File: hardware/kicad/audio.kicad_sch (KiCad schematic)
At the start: 0 parts

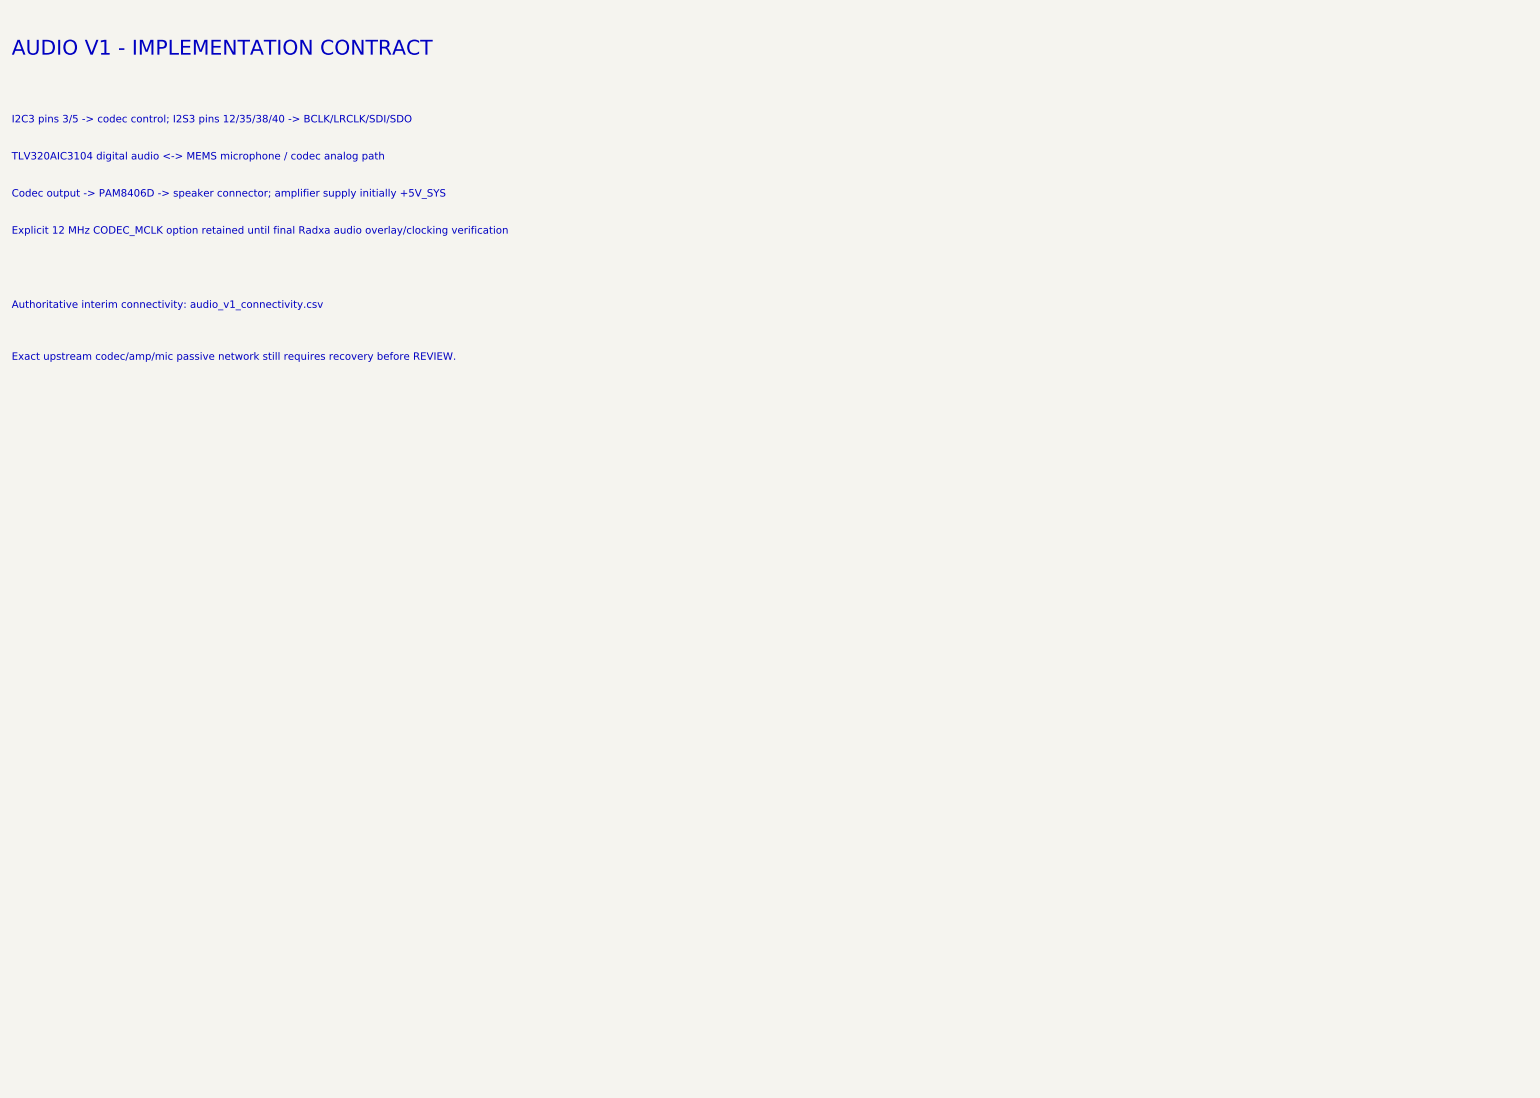
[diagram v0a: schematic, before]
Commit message: [verified] refactor(hardware): restore strict single-board Radxa port
Import the routed upstream Pollen Robot HAT as the active design, adapt the critical host nets for Radxa ZERO 3W, remove the divergent high-current redesign artifacts, and add regenerated baseline-aware KiCad validation.
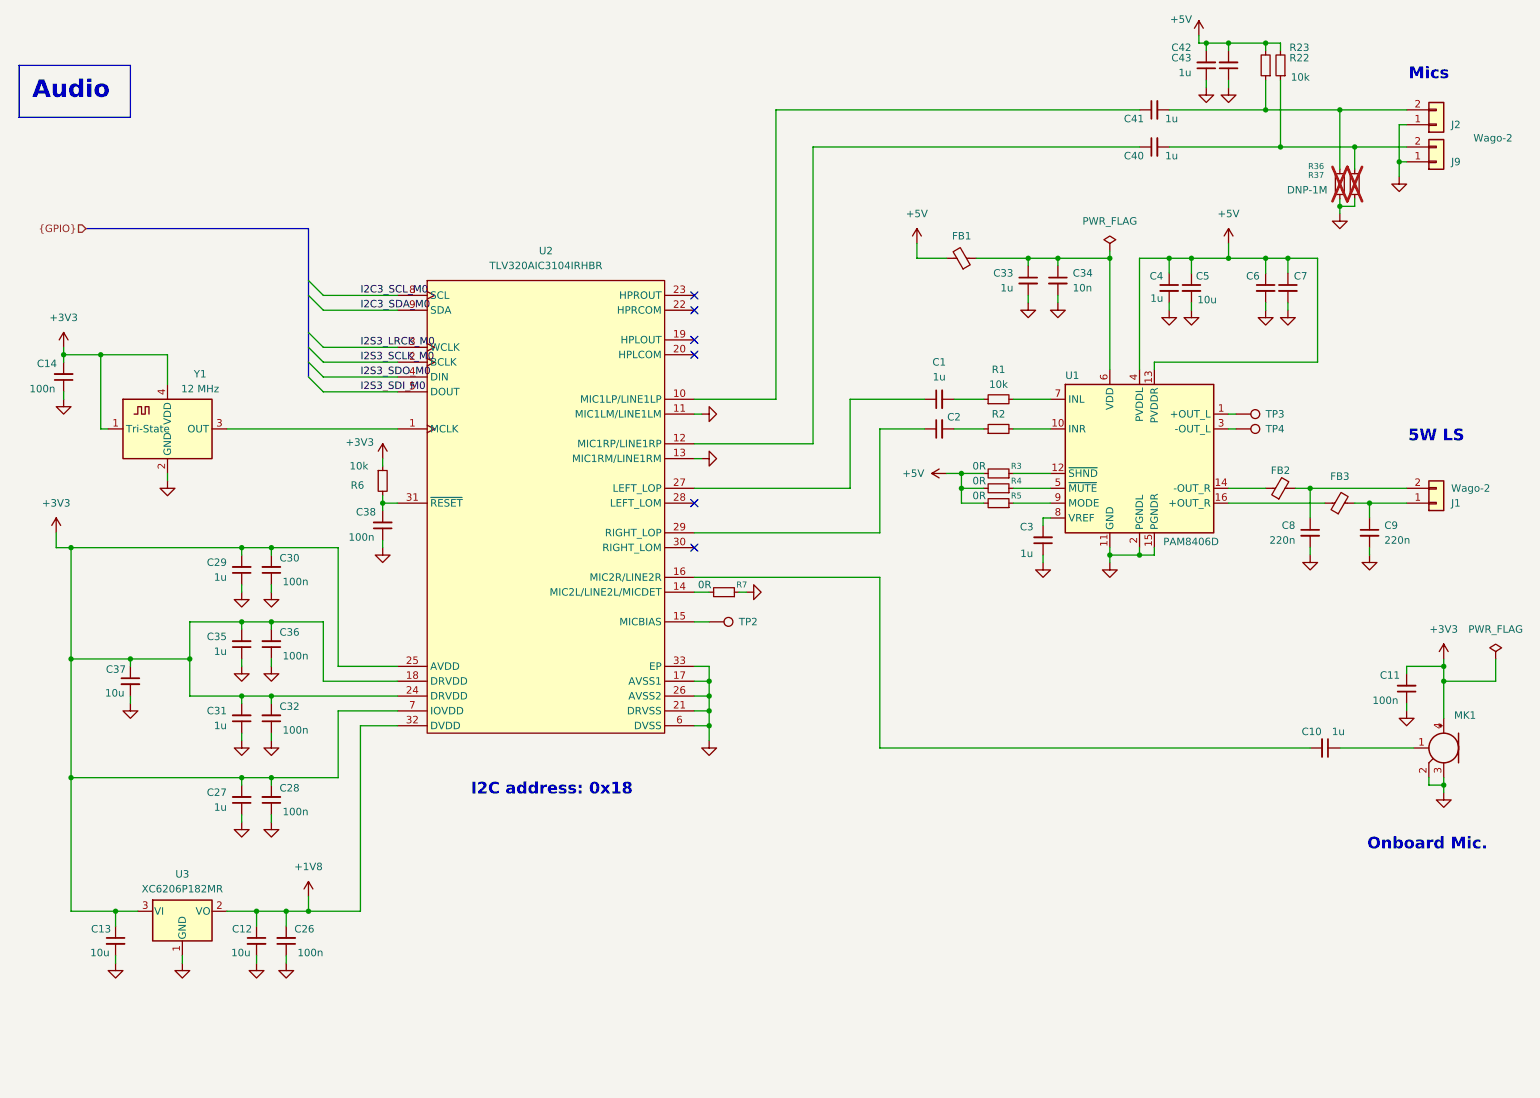
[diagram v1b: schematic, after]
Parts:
- added C1, C10, C2, C27, C29, C3, C31, C33, C35, C4, C40, C41, C42, C43, C6: 1u, Capacitor_SMD:C_0402_1005Metric, symbol Device:C_Small
- added C11, C14, C26, C28, C30, C32, C36, C38: 100n, Capacitor_SMD:C_0402_1005Metric, symbol Device:C_Small
- added C12, C13, C37, C5, C7: 10u, Capacitor_SMD:C_0603_1608Metric, symbol Device:C_Small
- added C34: 10n, Capacitor_SMD:C_0402_1005Metric, symbol Device:C_Small
- added C8, C9: 220n, Capacitor_SMD:C_0402_1005Metric, symbol Device:C_Small
- added FB1: 1.3A 600R@100MHz, Inductor_SMD:L_0402_1005Metric, symbol Device:FerriteBead_Small
- added FB2, FB3: 2A - 120R@100MHz, Inductor_SMD:L_0402_1005Metric, symbol Device:FerriteBead_Small
- added J1, J2, J9: Wago-2, LCSC_parts_lib:Wago_2059-302_998-403, symbol Connector_Generic:Conn_01x02
- added MK1: Microphone_MEMS, LCSC_parts_lib:MIC-SMD_4P-L2.8-W1.9-P1.84-TL, symbol Library_Pollen:Microphone_MEMS
- added R1, R2, R22, R23, R6: 10k, Resistor_SMD:R_0402_1005Metric, symbol Device:R_Small
- added R3, R4, R5, R7: 0R, Resistor_SMD:R_0402_1005Metric, symbol Device:R_Small
- added R36, R37: DNP-1M, Resistor_SMD:R_0402_1005Metric, symbol Device:R_Small
- added TP2, TP3, TP4: TestPoint, TestPoint:TestPoint_Loop_D2.50mm_Drill1.0mm_LowProfile, symbol Connector:TestPoint
- added U1: PAM8406D, Package_SO:SOIC-16_3.9x9.9mm_P1.27mm, symbol Amplifier_Audio:PAM8406D
- added U2: TLV320AIC3104IRHBR, Package_DFN_QFN:VQFN-32-1EP_5x5mm_P0.5mm_EP3.5x3.5mm, symbol Library_Pollen:TLV320AIC3104IRHBR
- added U3: XC6206P182MR, Package_TO_SOT_SMD:SOT-23-3, symbol Regulator_Linear:XC6206PxxxMR
- added Y1: 12 MHz, Oscillator:Oscillator_SMD_Abracon_ASDMB-4Pin_2.5x2.0mm, symbol Oscillator:ASCO
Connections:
- new net: C33.1, C34.1, FB1.1, U1.6 (VDD)
- new net: C1.1, U2.27 (LEFT_LOP)
- new net: C1.2, R1.1
- new net: C9.1, FB3.2, J1.1 (Pin_1)
- new net: C8.1, FB2.2, J1.2 (Pin_2)
- new net: U2.1 (MCLK), Y1.3 (OUT)
- new net: C10.1, MK1.1 (-)
- new net: C10.2, U2.16 (MIC2R/LINE2R)
- new net: C41.2, J2.2 (Pin_2), R22.1, R36.2
- new net: C38.2, R6.2, U2.31 (~{RESET})
- new net: C2.2, R2.1
- new net: R2.2, U1.10 (INR)
- new net: TP3.1, U1.1 (+OUT_L)
- new net: R5.1, U1.9 (MODE)
- new net: R1.2, U1.7 (INL)
- new net: C41.1, U2.10 (MIC1LP/LINE1LP)
- new net: C40.1, U2.12 (MIC1RP/LINE1RP)
- new net: C40.2, J9.2 (Pin_2), R23.1, R37.2
- new net: TP2.1, U2.15 (MICBIAS)
- new net: R3.1, U1.12 (~{SHND})
- new net: FB2.1, U1.14 (-OUT_R)
- new net: FB3.1, U1.16 (+OUT_R)
- new net: TP4.1, U1.3 (-OUT_L)
- new net: R4.1, U1.5 (~{MUTE})
- new net: C3.2, U1.8 (VREF)
- new net: R7.2, U2.14 (MIC2L/LINE2L/MICDET)
- new net: C2.1, U2.29 (RIGHT_LOP)
- new net +1V8: C12.1, C26.2, U2.32 (DVDD), U3.2 (VO)
- new net +3V3: C11.2, C13.1, C14.2, C27.2, C28.2, C29.2, C30.2, C31.2, C32.2, C35.2, C36.2, C37.1, MK1.4 (+), R6.1, U2.18 (DRVDD), U2.24 (DRVDD), U2.25 (AVDD), U2.7 (IOVDD), U3.3 (VI), Y1.1 (Tri-State), Y1.4 (VDD)
- new net +5V: C4.1, C42.2, C43.2, C5.1, C6.1, C7.1, FB1.2, R22.2, R23.2, R3.2, R4.2, R5.2, U1.13 (PVDDR), U1.4 (PVDDL)
- new net GND: C11.1, C12.2, C13.2, C14.1, C26.1, C27.1, C28.1, C29.1, C3.1, C30.1, C31.1, C32.1, C33.2, C34.2, C35.1, C36.1, C37.2, C38.1, C4.2, C42.1, C43.1, C5.2, C6.2, C7.2, C8.2, C9.2, J2.1 (Pin_1), J9.1 (Pin_1), MK1.2 (-), MK1.3 (-), R36.1, R37.1, R7.1, U1.11 (GND), U1.15 (PGNDR), U1.2 (PGNDL), U2.11 (MIC1LM/LINE1LM), U2.13 (MIC1RM/LINE1RM), U2.17 (AVSS1), U2.21 (DRVSS), U2.26 (AVSS2), U2.33 (EP), U2.6 (DVSS), U3.1 (GND), Y1.2 (GND)
- new net I2C3_SCL_M0: U2.8 (SCL)
- new net I2C3_SDA_M0: U2.9 (SDA)
- new net I2S3_LRCK_M0: U2.3 (WCLK)
- new net I2S3_SCLK_M0: U2.2 (BCLK)
- new net I2S3_SDI_M0: U2.5 (DOUT)
- new net I2S3_SDO_M0: U2.4 (DIN)
- no-connect marks 0 -> 6
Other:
- note added: "5W LS"
- note added: "I2C address: 0x18"
- note added: "Mics"
- note added: "Onboard Mic."
- note removed: "AUDIO V1 - IMPLEMENTATION CONTRACT"
- note removed: "Authoritative interim connectivity: audio_v1_connectivity.csv"
- note removed: "Codec output -> PAM8406D -> speaker connector; amplifier supply initially +5V_SYS"
- note removed: "Exact upstream codec/amp/mic passive network still requires recovery before REVIEW."
- note removed: "Explicit 12 MHz CODEC_MCLK option retained until final Radxa audio overlay/clocking verification"
- note removed: "I2C3 pins 3/5 -> codec control; I2S3 pins 12/35/38/40 -> BCLK/LRCLK/SDI/SDO"
- note removed: "TLV320AIC3104 digital audio <-> MEMS microphone / codec analog path"
- company: juper007 / DIY -> Pollen Robotics / Hugging Face
- title: Radxa ZERO 3W Robot HAT - Audio V1 -> Radxa ZERO 3W Robot HAT

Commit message: [verified] fix(hardware): correct power bias and default-off GPIO controls
Qualify Q2 land and gate rating, battery-bias LM5050 VS, and correct C39 identity. Add host-referenced active-low battery sensing and default-off amplifier control while preserving connector parity. Expand exact regression guards and complete BOM/position exports. Fabrication approval remains pending physical and runtime validation.
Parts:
- added Q4, Q5: BC847B, Package_TO_SOT_SMD:SOT-23, symbol Transistor_BJT:Q_NPN_BEC
- added R44, R45: 10k, Resistor_SMD:R_0402_1005Metric, symbol Device:R_Small
- added R46: 100k, Resistor_SMD:R_0402_1005Metric, symbol Device:R_Small
- R3: value 0R -> 10k; LCSC Part C17168 -> (none); Manufacturer_Name (none) -> Yageo; Manufacturer_Part_Number (none) -> RC0402FR-0710KL; Power Rating (none) -> 0.063W; Tolerance (none) -> 1%; Voltage Rating (none) -> 50V
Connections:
- net +5V: now also R44.2
- net GND: now also Q4.2 (E), Q5.2 (E), R46.2
- net AMP_SHDN: now reaches R3.1, U1.12 (~{SHND})
- net AMP_SHDN: now also Q4.3 (C)
- new net AMP_BASE: Q5.1 (B), R45.1, R46.1
- new net AMP_ENABLE: R45.2
- new net AMP_INHIBIT: Q4.1 (B), Q5.3 (C), R44.1
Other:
- note added: "Default OFF: J4.11 / AMP_ENABLE HIGH enables amplifier"
